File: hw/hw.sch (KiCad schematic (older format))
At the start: 44 parts, among them U1 74LS32, U10 74LS74, U2 Z80CPU, U3 74LS138, U4 74LS08, U5 CY7C199, U6 74LS299, U7 74HCT574, U8 74LS161, U9 74LS245, X1 CXO_DIP8

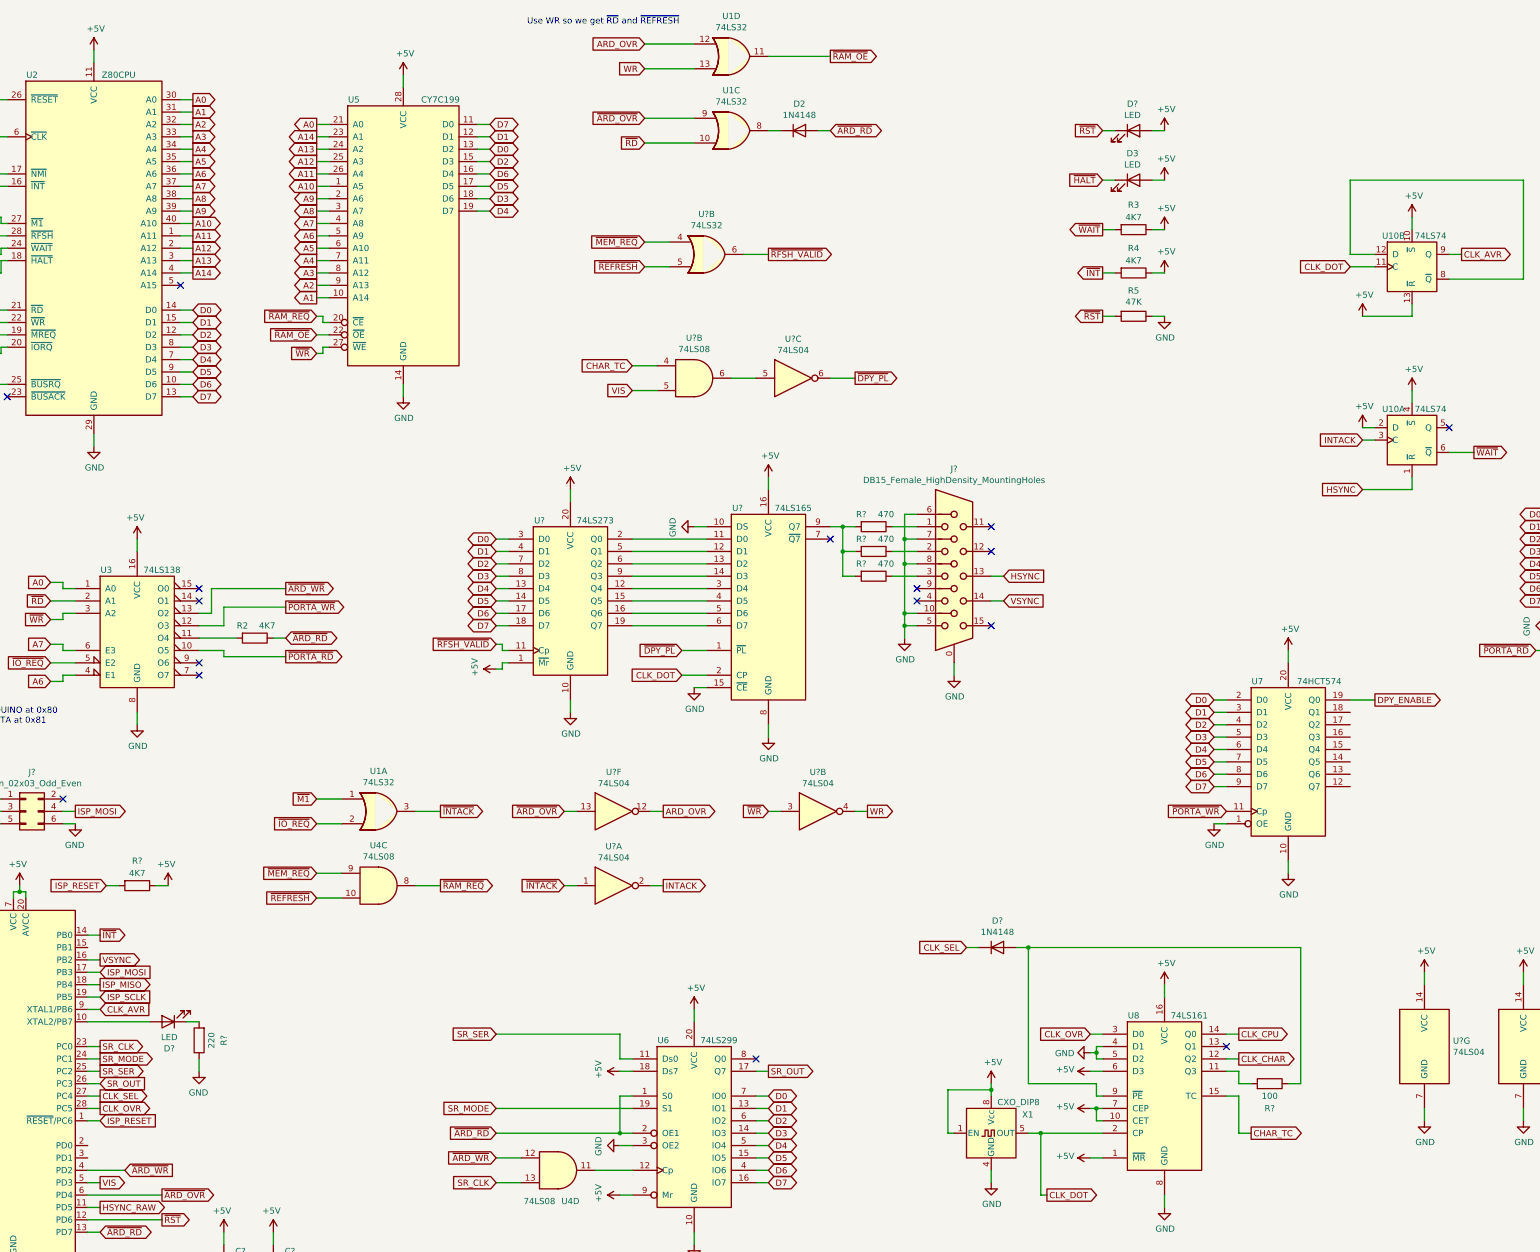
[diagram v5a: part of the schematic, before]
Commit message: PS2 data reading and UART
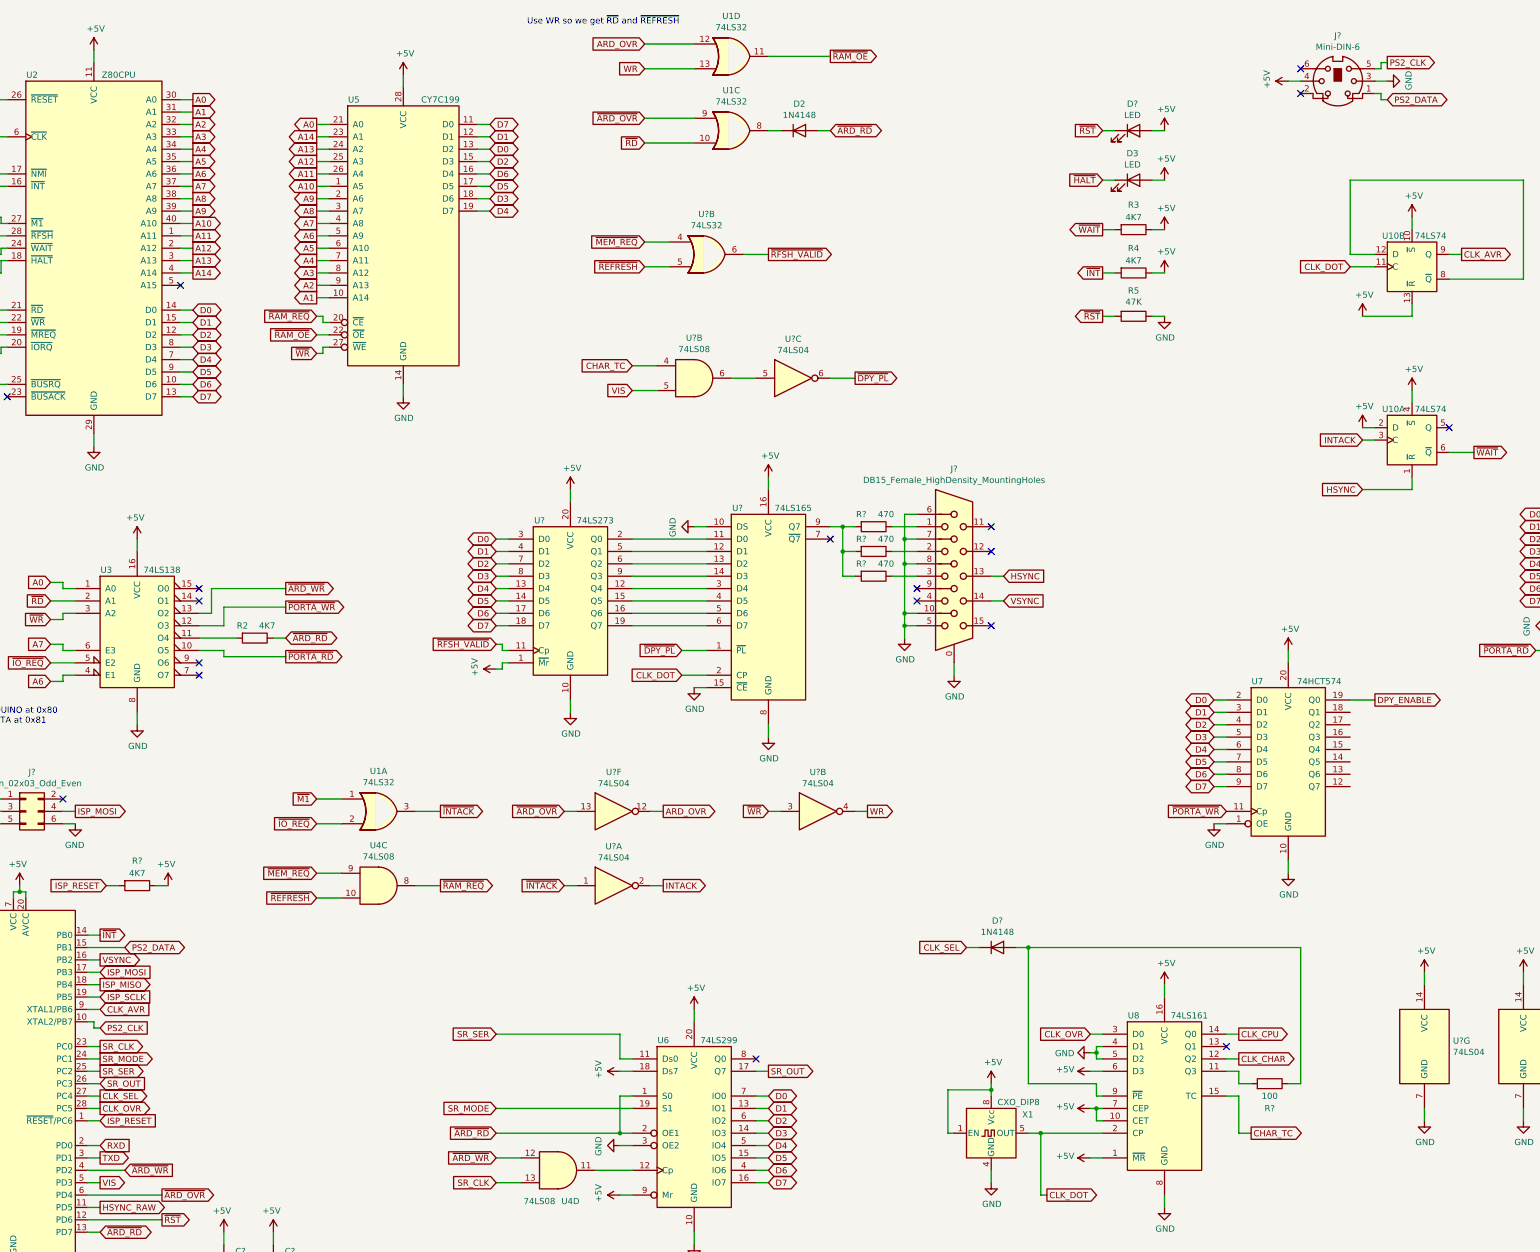
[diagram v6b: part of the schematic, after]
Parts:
- removed D?: LED, symbol Device:LED
- removed R?: 220, symbol Device:R
- added J?: Mini-DIN-6, symbol Connector:Mini-DIN-6
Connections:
- net +5V: now also J?.4
- net GND: now also J?.3
- net PS2_CLK: now reaches U?.10 (XTAL2/PB7)
- net PS2_CLK: now also J?.5
- net PS2_DATA: now reaches U?.15 (PB1)
- net PS2_DATA: now also J?.1
- net RXD: now reaches U?.2 (PD0)
- net TXD: now reaches U?.3 (PD1)
- no-connect marks 17 -> 19
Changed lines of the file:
@@
 Text Notes 15400 1750 0    50   ~ 0
 Open Question: sync VIS to CHAR_TC?
-$Comp
-L Device:LED D?
-U 1 1 5E7A4E6B
-P 2850 8700
-F 0 "D?" H 2841 8916 50  0000 C CNN
-F 1 "LED" H 2841 8825 50  0000 C CNN
-F 2 "" H 2850 8700 50  0001 C CNN
-F 3 "~" H 2850 8700 50  0001 C CNN
-	1    2850 8700
-	-1   0    0    1
-$EndComp
-Wire Wire Line
-	2200 8700 2700 8700
-$Comp
-L power:GND #PWR?
-U 1 1 5E7D7FFB
-P 3100 9100
-F 0 "#PWR?" H 3100 8850 50  0001 C CNN
-F 1 "GND" H 3105 8927 50  0000 C CNN
-F 2 "" H 3100 9100 50  0001 C CNN
-F 3 "" H 3100 9100 50  0001 C CNN
-	1    3100 9100
-	-1   0    0    -1
-$EndComp
-Wire Wire Line
-	3000 8700 3100 8700
-$Comp
-L Device:R R?
-U 1 1 5E80B2C2
-P 3100 8850
-F 0 "R?" V 2900 8850 50  0000 C CNN
-F 1 "220" V 3000 8850 50  0000 C CNN
-F 2 "" V 3030 8850 50  0001 C CNN
-F 3 "~" H 3100 8850 50  0001 C CNN
-	1    3100 8850
-	-1   0    0    1
-$EndComp
-Wire Wire Line
-	3100 9000 3100 9100
 Text GLabel 2500 9900 2    50   Input ~ 0
 ~ARD_WR
@@
 Wire Wire Line
 	6500 9600 6600 9600
+$Comp
+L Connector:Mini-DIN-6 J?
+U 1 1 5ECFB4A4
+P 12300 1100
+F 0 "J?" H 12300 1467 50  0000 C CNN
+F 1 "Mini-DIN-6" H 12300 1376 50  0000 C CNN
+F 2 "" H 12300 1100 50  0001 C CNN
+F 3 "http://service.powerdynamics.com/ec/Catalog17/Section%2011.pdf" H 12300 1100 50  0001 C CNN
+	1    12300 1100
+	1    0    0    -1
+$EndComp
+$Comp
+L power:+5V #PWR?
+U 1 1 5ECFB971
+P 11900 1100
+F 0 "#PWR?" H 11900 950 50  0001 C CNN
+F 1 "+5V" H 11915 1273 50  0000 C CNN
+F 2 "" H 11900 1100 50  0001 C CNN
+F 3 "" H 11900 1100 50  0001 C CNN
+	1    11900 1100
+	0    -1   -1   0
+$EndComp
+$Comp
+L power:GND #PWR?
+U 1 1 5ECFB9E4
+P 12700 1100
+F 0 "#PWR?" H 12700 850 50  0001 C CNN
+F 1 "GND" H 12705 927 50  0000 C CNN
+F 2 "" H 12700 1100 50  0001 C CNN
+F 3 "" H 12700 1100 50  0001 C CNN
+	1    12700 1100
+	0    -1   -1   0
+$EndComp
+Wire Wire Line
+	12600 1100 12700 1100
+Wire Wire Line
+	11900 1100 12000 1100
+Text GLabel 12700 1250 2    50   BiDi ~ 0
+PS2_DATA
+Wire Wire Line
+	12700 1250 12650 1250
+Wire Wire Line
+	12650 1250 12650 1200
+Wire Wire Line
+	12650 1200 12600 1200
+Text GLabel 12700 950  2    50   Output ~ 0
+PS2_CLK
+Wire Wire Line
+	12700 950  12650 950
+Wire Wire Line
+	12650 950  12650 1000
+Wire Wire Line
+	12650 1000 12600 1000
+NoConn ~ 12000 1000
+NoConn ~ 12000 1200
+Text GLabel 2300 8750 2    50   Input ~ 0
+PS2_CLK
+Text GLabel 2500 8100 2    50   BiDi ~ 0
+PS2_DATA
+Wire Wire Line
+	2300 8750 2250 8750
+Wire Wire Line
+	2250 8750 2250 8700
+Wire Wire Line
+	2250 8700 2200 8700
+Wire Wire Line
+	2500 8100 2200 8100
+Text GLabel 2300 9800 2    50   Output ~ 0
+TXD
+Text GLabel 2300 9700 2    50   Input ~ 0
+RXD
+Wire Wire Line
+	2300 9800 2200 9800
+Wire Wire Line
+	2300 9700 2200 9700
 $EndSCHEMATC

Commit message: simplifying hw
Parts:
- removed D3: LED, symbol Device:LED
- removed RN?: R_Network08_US, Resistor_THT:R_Array_SIP9, symbol Device:R_Network08_US
- removed U7: 74HCT574, symbol 74xx:74HCT574
- removed U9: 74LS245, symbol 74xx:74LS245
- removed U?: 74LS32, symbol 74xx:74LS32
- removed U?: 74LS273, symbol 74xx:74LS273
- added U?: 74LS74, symbol 74xx:74LS74
- added U?: 74LS32, symbol 74xx:74LS32
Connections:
- net ~PORTA_RD is gone; now on an unnamed net: U3.10 (O5)
- net +5V: now also U?.10 (~S), U?.13 (~R)
- net A0: no longer U3.1 (A0)
- net A5: now also U3.1 (A0)
- net CLK_CHAR: now also U?.11 (C)
- net D0: now also U?.11 (D0)
- net D1: now also U?.12 (D1)
- net D2: now also U?.13 (D2)
- net D3: now also U?.14 (D3)
- net D4: now also U?.3 (D4)
- net D5: now also U?.4 (D5)
- net D6: now also U?.5 (D6)
- net D7: now also U?.6 (D7)
- net VIS: now also U?.9 (Q); no longer U?.5 (PD3)
- net ~RAM_REQ: now also U?.6; no longer U4.8
- net A15: now reaches U2.5 (A15)
- net A15: now also U?.5
- net at R2.2: no longer U3.11 (O4)
- net ~PORTA_WR: no longer names the net of U3.12 (O3)
- new net: U4.8, U?.4
- new net VIS_RAW: U?.12 (D), U?.5 (PD3)
- no-connect marks 19 -> 21
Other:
- note added: "AVR at 0xa0-0xbf"
- note removed: "ARDUINO at 0x80\nPORTA at 0x81"
- note removed: "Open Question: sync VIS to CHAR_TC?"
- note removed: "Use WR so we get ~RD and ~REFRESH"
- moved on the sheet: D?, R1, R2, U2, U4C, U5

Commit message: start schematic tidy up
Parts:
- removed D?: LED, symbol Device:LED
- removed R3, R4: 4K7, symbol Device:R
- removed R5: 47K, symbol Device:R
- added R? (x3): 4K7, symbol Device:R
- J?: value Conn_02x03_Odd_Even -> ISP
- J?: value Mini-DIN-6 -> Keyboard
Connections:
- net +5V: now also R?.2, R?.2, R?.2; no longer U2.17 (~NMI~)
- net ~ARD_OVR: no longer U?.6 (PD4)
- net ~ARD_RD: no longer R2.1, U6.1 (S0), U6.2 (OE1), U?.13 (PD7)
- net ~INT: now also R?.1
- net ~RST: now also R?.1
- net ~BUSACK: now reaches U2.23 (~BUSACK~)
- net ~BUSRQ: now reaches R1.1, U2.25 (~BUSRQ~)
- net WR: no longer names the net of U1.13, U?.4
- net ~ARD_WR renamed ~AVR_WR
- new net ~AVR_OVR: U?.6 (PD4)
- new net ~AVR_RD: R2.1, U6.1 (S0), U6.2 (OE1), U?.13 (PD7)
- new net ~NMI: R?.1, U2.17 (~NMI~)
- no-connect marks 21 -> 20
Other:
- note added: "AVR Control Bus"
- note added: "Address Bus"
- note added: "Data Bus"
- moved on the sheet: C?, D2, D?, J?, R1, R2, R?, RN?, U10A, U10B, U1A, U1C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
